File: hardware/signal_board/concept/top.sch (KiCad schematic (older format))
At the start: 0 parts

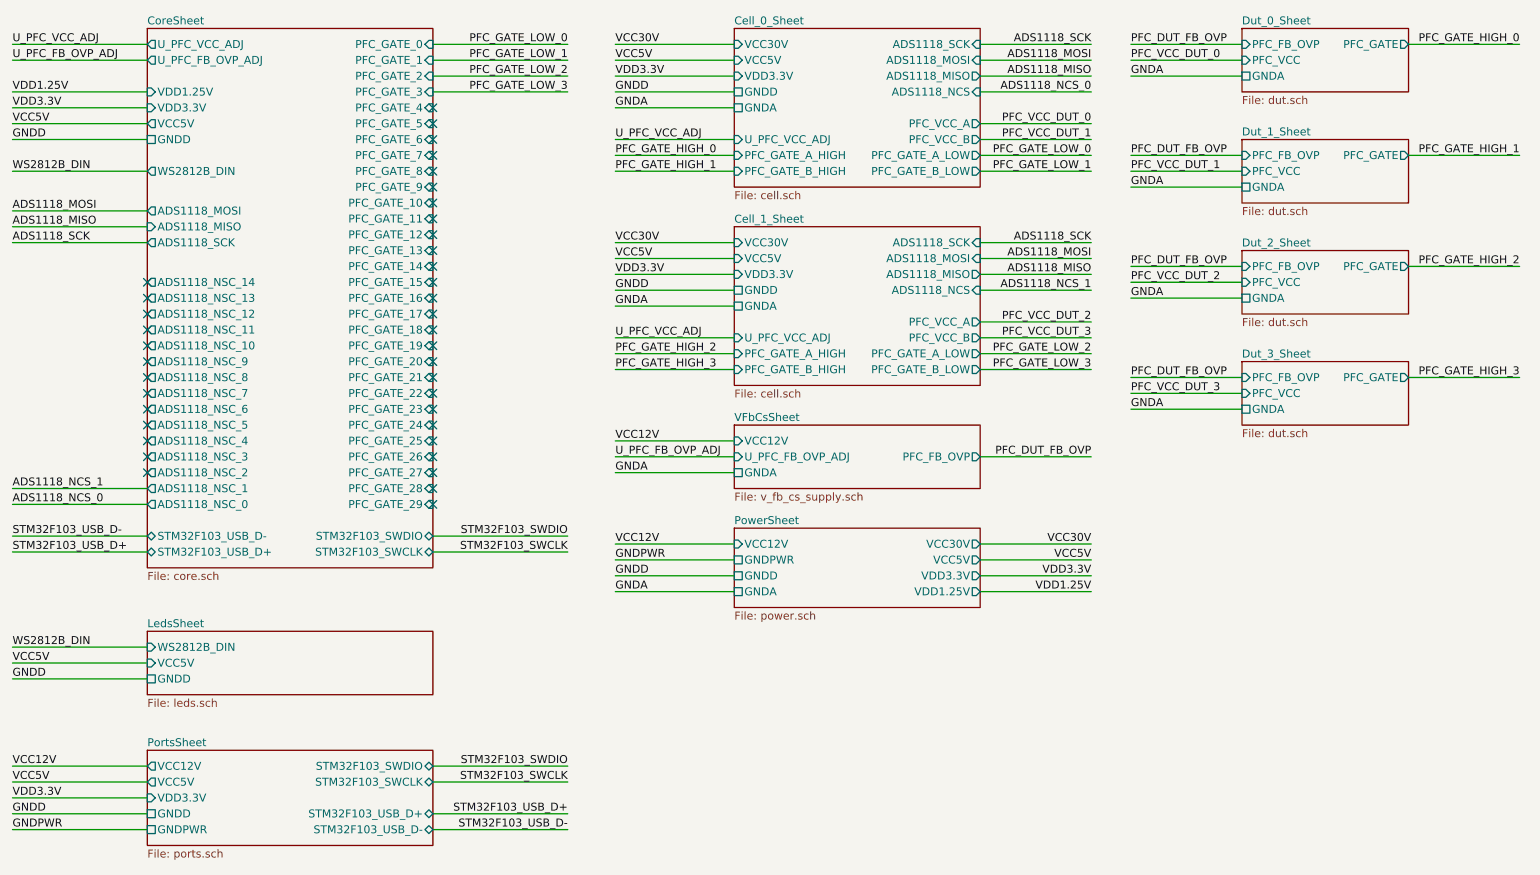
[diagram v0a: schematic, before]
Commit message: Add priduction board
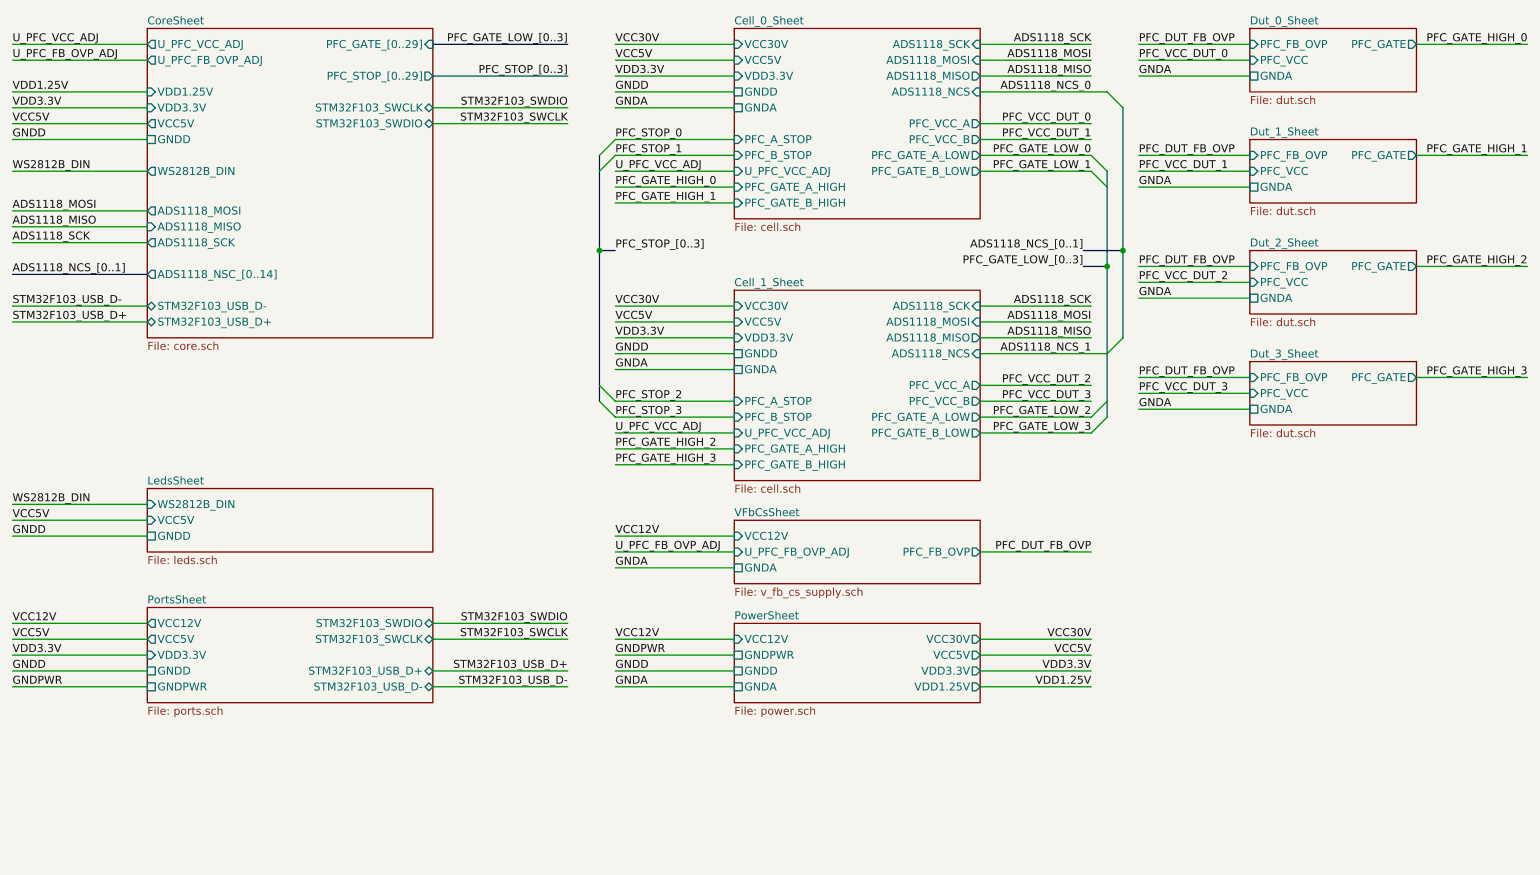
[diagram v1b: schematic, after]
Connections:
- no-connect marks 39 -> 0
